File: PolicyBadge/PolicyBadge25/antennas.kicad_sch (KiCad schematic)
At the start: 8 parts

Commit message: Released version of PCB
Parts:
- removed R11, R17: R, Capacitor_SMD:C_0402_1005Metric, symbol Device:R
- added Z11, Z8: 0Ω, imported:R0402, symbol JLCPCB:0402WGJ0000TCE
- Z10: renamed from R16; now not fitted; now left out of the parts list
- Z12: renamed from R18; now not fitted; now left out of the parts list
- Z7: renamed from R10; now not fitted; now left out of the parts list
- Z9: renamed from R12; now not fitted; now left out of the parts list
- renumbered AE4 to AE1, AE5 to AE2
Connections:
- net Feed_Point_2.4GHz: now also Z11.1
- net Feed_Point_915MHz: now also Z8.1
- net at AE2.1 (A), Z12.1: now also Z11.2
- net at AE1.1 (A), Z9.1: now also Z8.2

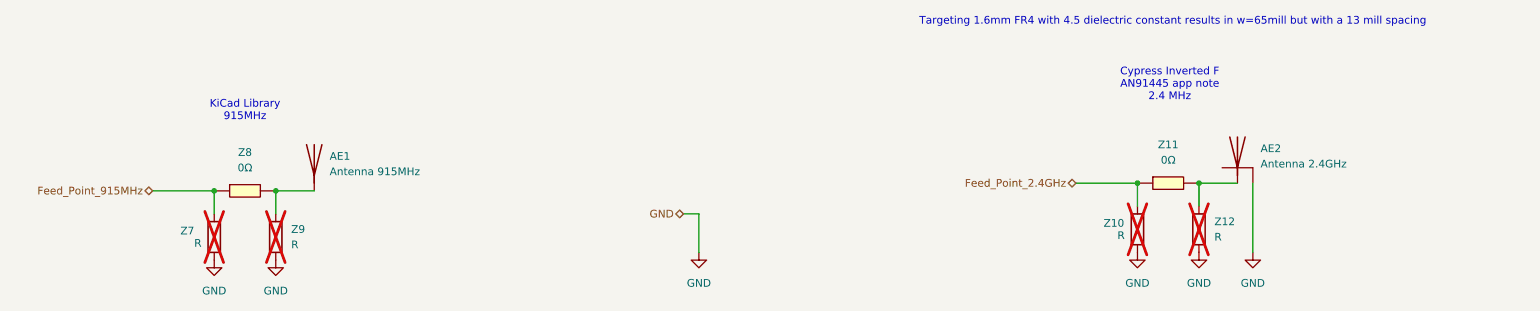
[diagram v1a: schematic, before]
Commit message: Lots of changes, laying out board for board shape
Updated switches
Added headers for XAIO
Fixed Batt Connector polarity
10K pullup on int
Batt monitor resistor divider
Fix buzzer trace
XAIO footprint spacing
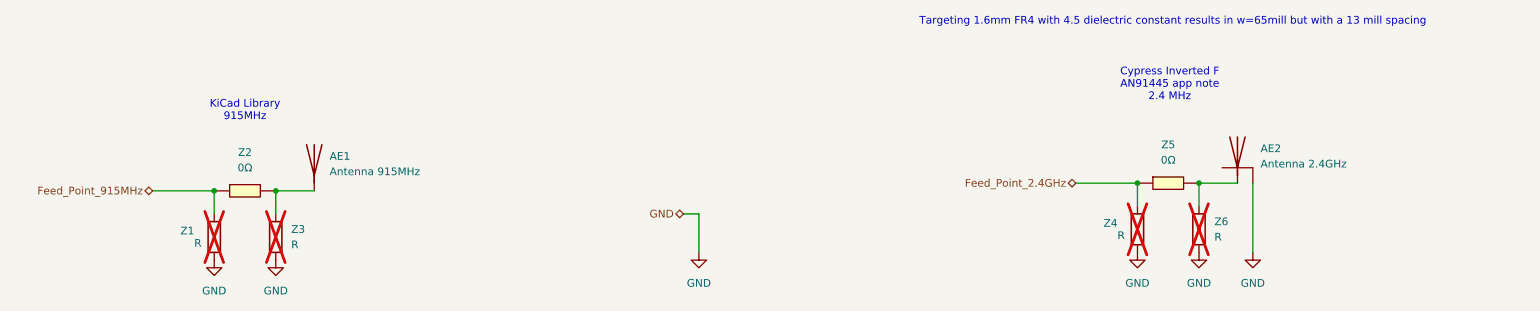
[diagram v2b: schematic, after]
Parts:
- renumbered Z7 to Z1, Z8 to Z2, Z9 to Z3, Z10 to Z4, Z11 to Z5, Z12 to Z6
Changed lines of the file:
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@@
 		(dnp no)
 		(fields_autoplaced yes)
-		(property "Reference" "#PWR029"
+		(property "Reference" "#PWR034"
 			(at 139.7 152.4 0)
 			(effects
@@
 			(project "PolicyBadge25"
 				(path "/3911717a-8f19-42c2-8f04-ebfae4e12db6/3596fef3-9133-4061-be50-a3314fca7315"
-					(reference "#PWR029")
+					(reference "#PWR034")
 					(unit 1)
 				)
@@
 		(dnp no)
 		(fields_autoplaced yes)
-		(property "Reference" "#PWR031"
+		(property "Reference" "#PWR036"
 			(at 222.25 152.4 0)
 			(effects
@@
 			(project "PolicyBadge25"
 				(path "/3911717a-8f19-42c2-8f04-ebfae4e12db6/3596fef3-9133-4061-be50-a3314fca7315"
-					(reference "#PWR031")
+					(reference "#PWR036")
 					(unit 1)
 				)
@@
 		(dnp yes)
 		(fields_autoplaced yes)
-		(property "Reference" "Z12"
+		(property "Reference" "Z6"
 			(at 224.79 140.9699 0)
 			(effects
@@
 			(project "PolicyBadge25"
 				(path "/3911717a-8f19-42c2-8f04-ebfae4e12db6/3596fef3-9133-4061-be50-a3314fca7315"
-					(reference "Z12")
+					(reference "Z6")
 					(unit 1)
 				)
@@
 		(dnp no)
 		(fields_autoplaced yes)
-		(property "Reference" "#PWR030"
+		(property "Reference" "#PWR035"
 			(at 212.09 152.4 0)
 			(effects
@@
 			(project "PolicyBadge25"
 				(path "/3911717a-8f19-42c2-8f04-ebfae4e12db6/3596fef3-9133-4061-be50-a3314fca7315"
-					(reference "#PWR030")
+					(reference "#PWR035")
 					(unit 1)
 				)
@@
 		(dnp no)
 		(fields_autoplaced yes)
-		(property "Reference" "Z8"
+		(property "Reference" "Z2"
 			(at 64.77 129.54 0)
 			(effects
@@
 			(project ""
 				(path "/3911717a-8f19-42c2-8f04-ebfae4e12db6/3596fef3-9133-4061-be50-a3314fca7315"
-					(reference "Z8")
+					(reference "Z2")
 					(unit 1)
 				)
@@
 		(dnp no)
 		(fields_autoplaced yes)
-		(property "Reference" "#PWR032"
+		(property "Reference" "#PWR037"
 			(at 231.14 152.4 0)
 			(effects
@@
 			(project "PolicyBadge25"
 				(path "/3911717a-8f19-42c2-8f04-ebfae4e12db6/3596fef3-9133-4061-be50-a3314fca7315"
-					(reference "#PWR032")
+					(reference "#PWR037")
 					(unit 1)
 				)
@@
 		(on_board yes)
 		(dnp yes)
-		(property "Reference" "Z10"
+		(property "Reference" "Z4"
 			(at 206.502 141.224 0)
 			(effects
@@
 			(project "PolicyBadge25"
 				(path "/3911717a-8f19-42c2-8f04-ebfae4e12db6/3596fef3-9133-4061-be50-a3314fca7315"
-					(reference "Z10")
+					(reference "Z4")
 					(unit 1)
 				)
@@
 		(dnp no)
 		(fields_autoplaced yes)
-		(property "Reference" "Z11"
+		(property "Reference" "Z5"
 			(at 217.17 128.27 0)
 			(effects
@@
 			(project "PolicyBadge25"
 				(path "/3911717a-8f19-42c2-8f04-ebfae4e12db6/3596fef3-9133-4061-be50-a3314fca7315"
-					(reference "Z11")
+					(reference "Z5")
 					(unit 1)
 				)
@@
 		(dnp no)
 		(fields_autoplaced yes)
-		(property "Reference" "#PWR028"
+		(property "Reference" "#PWR033"
 			(at 69.85 153.67 0)
 			(effects
@@
 			(project "PolicyBadge25"
 				(path "/3911717a-8f19-42c2-8f04-ebfae4e12db6/3596fef3-9133-4061-be50-a3314fca7315"
-					(reference "#PWR028")
+					(reference "#PWR033")
 					(unit 1)
 				)
@@
 		(on_board yes)
 		(dnp yes)
-		(property "Reference" "Z7"
+		(property "Reference" "Z1"
 			(at 54.102 142.494 0)
 			(effects
@@
 			(project "PolicyBadge25"
 				(path "/3911717a-8f19-42c2-8f04-ebfae4e12db6/3596fef3-9133-4061-be50-a3314fca7315"
-					(reference "Z7")
+					(reference "Z1")
 					(unit 1)
 				)
@@
 		(dnp yes)
 		(fields_autoplaced yes)
-		(property "Reference" "Z9"
+		(property "Reference" "Z3"
 			(at 72.39 142.2399 0)
 			(effects
@@
 			(project "PolicyBadge25"
 				(path "/3911717a-8f19-42c2-8f04-ebfae4e12db6/3596fef3-9133-4061-be50-a3314fca7315"
-					(reference "Z9")
+					(reference "Z3")
 					(unit 1)
 				)
@@
 		(dnp no)
 		(fields_autoplaced yes)
-		(property "Reference" "#PWR027"
+		(property "Reference" "#PWR032"
 			(at 59.69 153.67 0)
 			(effects
@@
 			(project "PolicyBadge25"
 				(path "/3911717a-8f19-42c2-8f04-ebfae4e12db6/3596fef3-9133-4061-be50-a3314fca7315"
-					(reference "#PWR027")
-					(unit 1)
-				)
+					(reference "#PWR032")
+					(unit 1)
+				)
